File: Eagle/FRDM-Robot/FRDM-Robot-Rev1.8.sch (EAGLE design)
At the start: 49 parts, among them IC1 DRV8835, Q2 IRF9321PbF

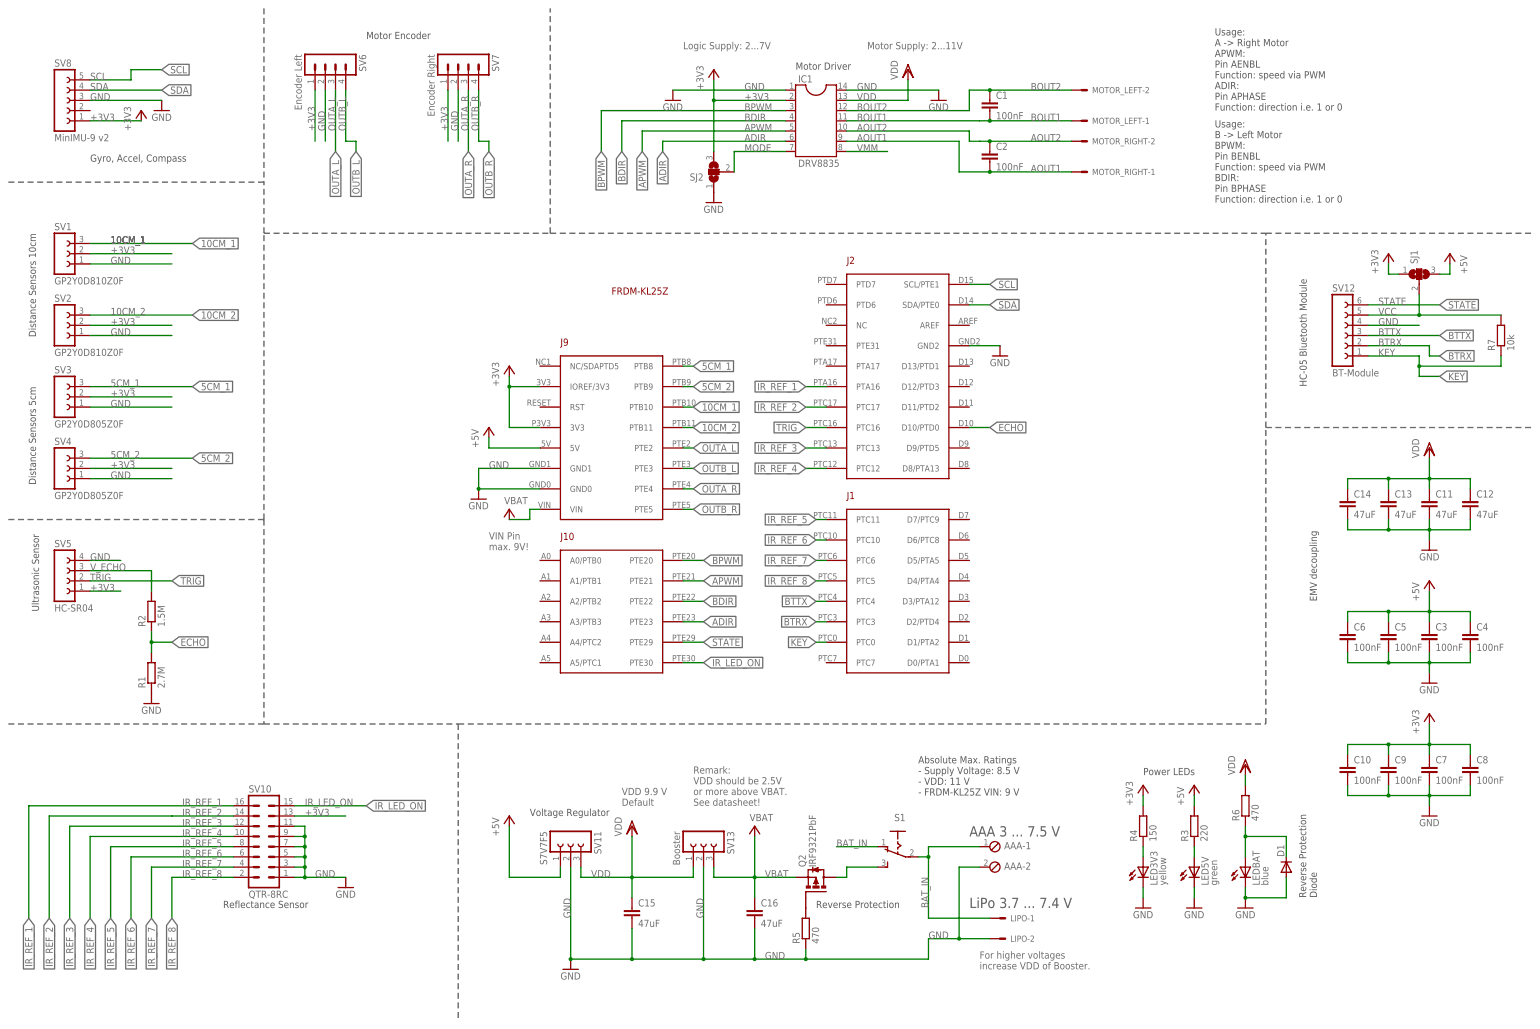
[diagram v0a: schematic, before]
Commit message: moved to sub folders
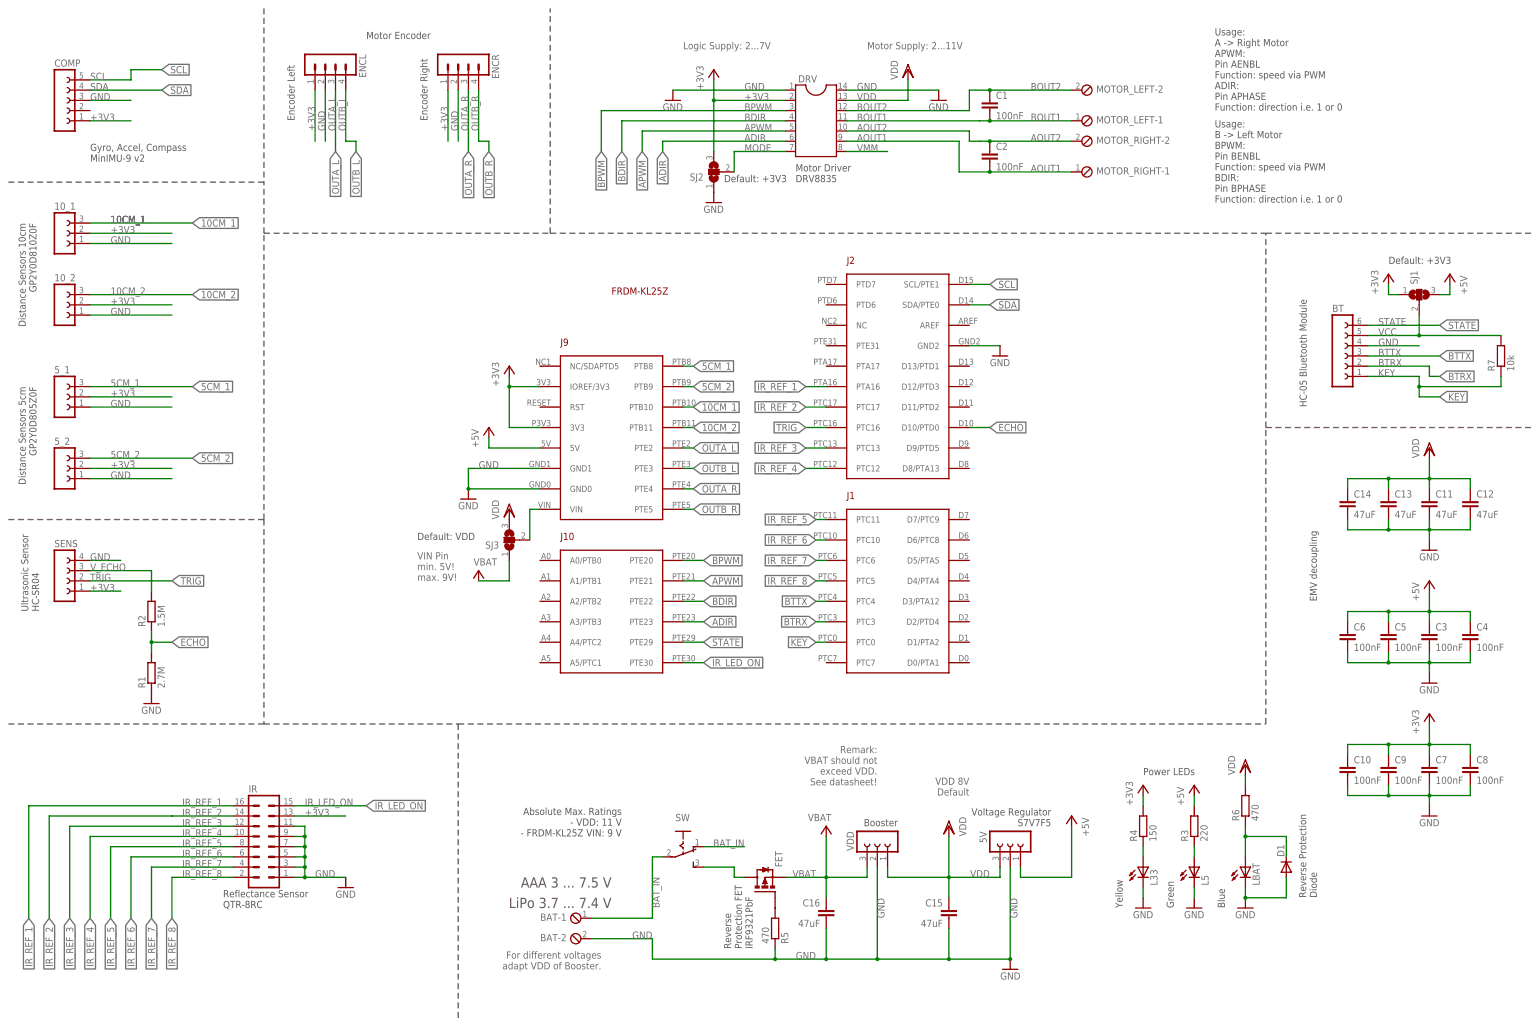
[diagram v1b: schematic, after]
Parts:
- removed AAA: (no value), con-phoenix-254:MPT2
- removed LIPO: (no value), con-molex:KK-156-2
- removed Q2: IRF9321PbF, transistor-power-IRF:P-MOSFET-SO8
- removed S1: (no value), switch-SPDT:KNITTER-MFP106D
- removed SV1, SV2: GP2Y0D810Z0F, con-lsta-Extended:FE03-1
- removed SV10: QTR-8RC, con-lstb:MA08-2
- removed SV11: S7V7F5, con-lsta-Extended:FE03-1
- removed SV12: BT-Module, con-lsta:FE06-1
- removed SV13: Booster, con-lsta-Extended:FE03-1
- added 10_1, 10_2, 5V, VDD: (no value), con-lsta-Extended:FE03-1
- added BAT: (no value), con-phoenix-254:MPT2
- added BT: (no value), con-lsta:FE06-1
- added FET: (no value), transistor-power-IRF-FRDM:P-MOSFET-SO8
- added IR: (no value), con-lstb-Extended:MA08-2
- added SJ3: (no value), jumper:SJ2W
- added SW: (no value), switch-SPDT:KNITTER-MFP106D
- 5_1, 5_2: value GP2Y0D805Z0F -> (none)
- COMP: value MinIMU-9 v2 -> (none)
- DRV: value DRV8835 -> (none)
- ENCL: value Encoder Left -> (none)
- ENCR: value Encoder Right -> (none)
- FRDM1: value FRDM-KL25ZARDUINO -> (none)
- L33: value yellow -> (none)
- L5: value green -> (none)
- LBAT: value blue -> (none)
- MOTOR_LEFT, MOTOR_RIGHT: device con-molex:KK-156-2 -> con-phoenix-254:MPT2
- SENS: value HC-SR04 -> (none)
- renumbered IC1 to DRV, LED3V3 to L33, LED5V to L5, LEDBAT to LBAT, SV3 to 5_1, SV4 to 5_2, SV5 to SENS, SV6 to ENCL, SV7 to ENCR, SV8 to COMP
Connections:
- removed net V+: FRDM1.VIN
- new net VIN: FRDM1.VIN, SJ3.2
- net +3V3: now also 10_1.2, 10_2.2, IR.13; no longer SV1.2, SV10.13, SV2.2
- net +5V: now also 5V.1; no longer SV11.1
- net 10CM_1: now also 10_1.3; no longer SV1.3
- net 10CM_2: now also 10_2.3; no longer SV2.3
- net AOUT1: now also MOTOR_RIGHT-1.1; no longer MOTOR_RIGHT-1.S
- net AOUT2: now also MOTOR_RIGHT-2.1; no longer MOTOR_RIGHT-2.S
- net BAT-FET: now also FET.D, SW.S; no longer Q2.D, S1.S
- net BAT_IN: now also BAT-1.1, SW.O, SW.P; no longer AAA-1.1, LIPO-1.S, S1.O, S1.P
- net BOUT1: now also MOTOR_LEFT-1.1; no longer MOTOR_LEFT-1.S
- net BOUT2: now also MOTOR_LEFT-2.1; no longer MOTOR_LEFT-2.S
- net BTRX: now also BT.2; no longer SV12.2
- net BTTX: now also BT.3; no longer SV12.3
- net GND: now also 10_1.1, 10_2.1, 5V.2, BAT-2.1, BT.4, IR.1, IR.11, IR.3, IR.5, IR.7, IR.9, VDD.2; no longer AAA-2.1, LIPO-2.S, SV1.1, SV10.1, SV10.11, SV10.3, SV10.5, SV10.7, SV10.9, SV11.2, SV12.4, SV13.2, SV2.1
- net IR_LED_ON: now also IR.15; no longer SV10.15
- net IR_REF_1: now also IR.16; no longer SV10.16
- net IR_REF_2: now also IR.14; no longer SV10.14
- net IR_REF_3: now also IR.12; no longer SV10.12
- net IR_REF_4: now also IR.10; no longer SV10.10
- net IR_REF_5: now also IR.8; no longer SV10.8
- net IR_REF_6: now also IR.6; no longer SV10.6
- net IR_REF_7: now also IR.4; no longer SV10.4
- net IR_REF_8: now also IR.2; no longer SV10.2
- net KEY: now also BT.1; no longer SV12.1
- net N$5: now also FET.G; no longer Q2.G
- net STATE: now also BT.6; no longer SV12.6
- net VBAT: now also FET.S, SJ3.1, VDD.3; no longer Q2.S, SV13.3
- net VCC: now also BT.5; no longer SV12.5
- net VDD: now also 5V.3, SJ3.3, VDD.1; no longer SV11.3, SV13.1
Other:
- note added: "Absolute Max. Ratings - VDD: 11 V - FRDM-KL25Z VIN: 9 V"
- note added: "Blue"
- note added: "Booster"
- note added: "Default: +3V3"
- note added: "Default: VDD"
- note added: "Distance Sensors 10cm GP2Y0D810Z0F"
- note added: "Distance Sensors 5cm GP2Y0D805Z0F"
- note added: "Encoder Left"
- note added: "Encoder Right"
- note added: "For different voltages adapt VDD of Booster."
- note added: "Green"
- note added: "Gyro, Accel, Compass MinIMU-9 v2"
- note added: "Motor Driver DRV8835"
- note added: "Reflectance Sensor QTR-8RC"
- note added: "Remark: VBAT should not exceed VDD. See datasheet!"
- note added: "Reverse Protection FET IRF9321PbF"
- note added: "Ultrasonic Sensor HC-SR04"
- note added: "VDD 8V Default"
- note added: "VIN Pin min. 5V! max. 9V!"
- note added: "Voltage Regulator S7V7F5"
- note added: "Yellow"
- note removed: "Absolute Max. Ratings - Supply Voltage: 8.5 V - VDD: 11 V - FRDM-KL25Z VIN: 9 V"
- note removed: "Distance Sensors 10cm"
- note removed: "Distance Sensors 5cm"
- note removed: "For higher voltages increase VDD of Booster."
- note removed: "Gyro, Accel, Compass"
- note removed: "Motor Driver"
- note removed: "Reflectance Sensor"
- note removed: "Remark: VDD should be 2.5V or more above VBAT. See datasheet!"
- note removed: "Reverse Protection"
- note removed: "Ultrasonic Sensor"
- note removed: "VDD 9.9 V Default"
- note removed: "VIN Pin max. 9V!"
- note removed: "Voltage Regulator"
- moved on the sheet: C15, C16, R5, R7, SJ1
